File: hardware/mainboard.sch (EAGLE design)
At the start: 80 parts, among them IC1 ATMEGA328, IC10 HM628512A_DIL32, IC11 HM628512A_DIL32, IC12 7805TV, IC13 DS1210, IC14 6N138, IC3 TLC074, IC4 74HCT04N, IC5 74HC238N, IC6 74HCT573N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

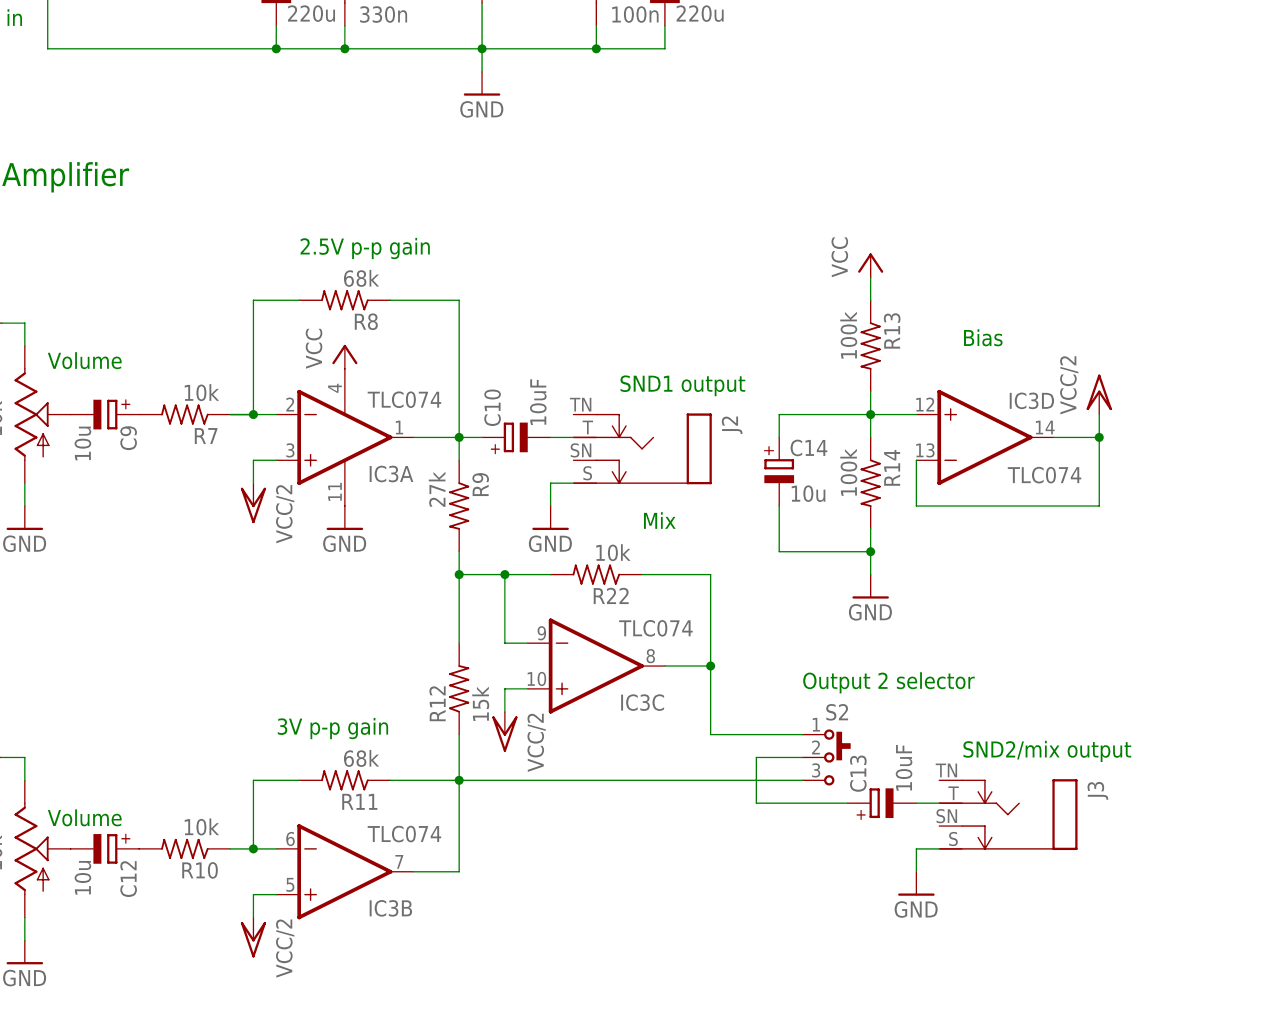
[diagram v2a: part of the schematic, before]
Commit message: Add small caps in feedback path for noise reduction and stability
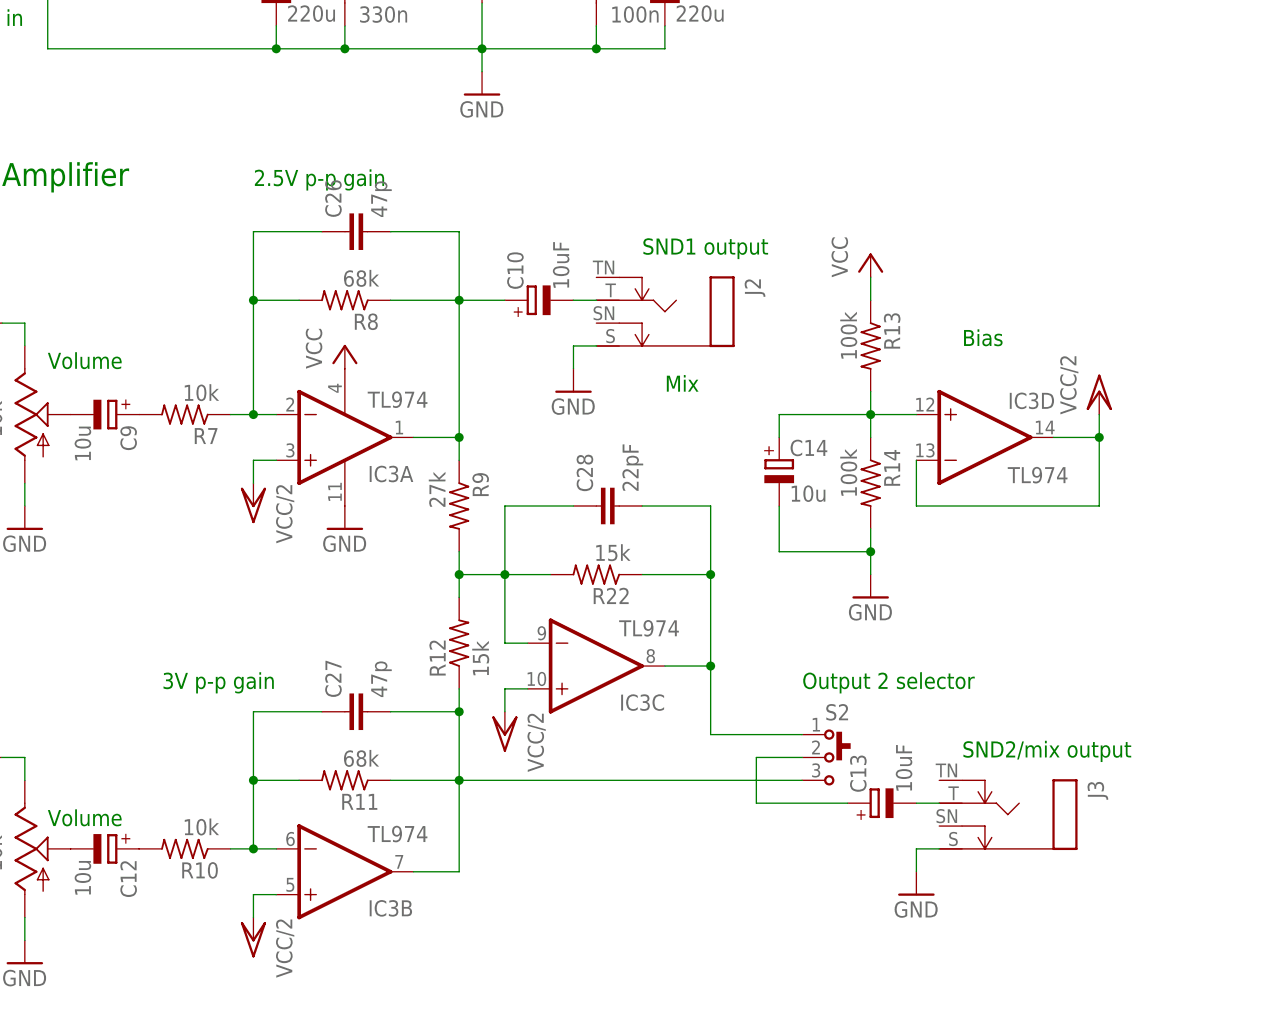
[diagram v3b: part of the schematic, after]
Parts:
- added C26, C27: 47p, capacitor-wima:C2.5/2
- added C28: 22pF, capacitor-wima:C2.5/2
- IC3: value TLC074 -> TL974
- R22: value 10k -> 15k
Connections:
- net N$14: now also C28.1
- net N$18: now also C26.1
- net N$24: now also C27.1
- net N$25: now also C26.2
- net N$26: now also C28.2
- net N$36: now also C27.2
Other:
- moved on the sheet: C10, J2, R12
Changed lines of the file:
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@@
 <part name="R12" library="rcl" deviceset="R-US_" device="0207/7" value="15k"/>
 <part name="R9" library="rcl" deviceset="R-US_" device="0207/7" value="27k"/>
-<part name="IC3" library="linear" deviceset="TL074" device="P" value="TLC074"/>
+<part name="IC3" library="linear" deviceset="TL074" device="P" value="TL974"/>
 <part name="R8" library="rcl" deviceset="R-US_" device="0207/7" value="68k"/>
 <part name="R7" library="rcl" deviceset="R-US_" device="0207/7" value="10k"/>
@@
 <part name="R16" library="rcl" deviceset="R-US_" device="0207/7" value="4.7k"/>
 <part name="D1" library="gm-diodes" deviceset="1N400X" device=".3"/>
-<part name="R22" library="rcl" deviceset="R-US_" device="0207/7" value="10k"/>
+<part name="R22" library="rcl" deviceset="R-US_" device="0207/7" value="15k"/>
 <part name="P+7" library="supply1" deviceset="VCC/2" device=""/>
+<part name="C26" library="capacitor-wima" deviceset="C" device="2.5/2" value="47p"/>
+<part name="C27" library="capacitor-wima" deviceset="C" device="2.5/2" value="47p"/>
+<part name="C28" library="capacitor-wima" deviceset="C" device="2.5/2" value="22pF"/>
 </parts>
 <sheets>
@@
 <text x="116.84" y="-96.52" size="2.54" layer="91">FIltering caps</text>
 <text x="55.88" y="-119.38" size="1.778" layer="91">SND2/mix output</text>
-<text x="17.78" y="-78.74" size="1.778" layer="91">SND1 output</text>
+<text x="20.32" y="-63.5" size="1.778" layer="91">SND1 output</text>
 <text x="-68.58" y="-38.1" size="1.778" layer="91">8V or higher DC in</text>
 <text x="-45.72" y="-76.2" size="1.778" layer="91">Volume</text>
 <text x="-45.72" y="-127" size="1.778" layer="91">Volume</text>
 <text x="38.1" y="-111.76" size="1.778" layer="91">Output 2 selector</text>
-<text x="-17.78" y="-63.5" size="1.778" layer="91">2.5V p-p gain</text>
-<text x="-20.32" y="-116.84" size="1.778" layer="91">3V p-p gain</text>
-<text x="20.32" y="-93.98" size="1.778" layer="91">Mix</text>
+<text x="-22.86" y="-55.88" size="1.778" layer="91">2.5V p-p gain</text>
+<text x="-33.02" y="-111.76" size="1.778" layer="91">3V p-p gain</text>
+<text x="22.86" y="-78.74" size="1.778" layer="91">Mix</text>
 <text x="304.8" y="-152.4" size="2.54" layer="91" font="vector">4</text>
 <text x="228.6" y="-132.08" size="2.54" layer="91" font="vector">(c) 2014-2015 Johan Fjeldtvedt</text>
@@
 <attribute name="VALUE" x="160.782" y="29.21" size="1.778" layer="96" rot="R90"/>
 </instance>
-<instance part="R12" gate="G$1" x="0" y="-111.76" rot="R90"/>
+<instance part="R12" gate="G$1" x="0" y="-106.68" rot="R90"/>
 <instance part="R9" gate="G$1" x="0" y="-91.44" smashed="yes" rot="R270">
 <attribute name="NAME" x="1.4986" y="-87.63" size="1.778" layer="95" rot="R270"/>
@@
 <instance part="R8" gate="G$1" x="-12.7" y="-68.58" rot="R180"/>
 <instance part="R7" gate="G$1" x="-30.48" y="-81.28" rot="R180"/>
-<instance part="C10" gate="G$1" x="5.08" y="-83.82" rot="R90"/>
+<instance part="C10" gate="G$1" x="7.62" y="-68.58" rot="R90"/>
 <instance part="R11" gate="G$1" x="-12.7" y="-121.92" rot="R180"/>
 <instance part="R10" gate="G$1" x="-30.48" y="-129.54" rot="R180"/>
@@
 <instance part="H3" gate="G$1" x="142.24" y="-149.86"/>
 <instance part="H4" gate="G$1" x="142.24" y="-154.94"/>
-<instance part="J2" gate="G$1" x="25.4" y="-86.36" rot="R180"/>
+<instance part="J2" gate="G$1" x="27.94" y="-71.12" rot="R180"/>
 <instance part="J3" gate="G$1" x="66.04" y="-127" rot="R180"/>
 <instance part="VR1" gate="L" x="-48.26" y="-81.28"/>
@@
 <attribute name="NAME" x="40.64" y="-115.2525" size="1.778" layer="95" ratio="10"/>
 </instance>
-<instance part="GND22" gate="1" x="10.16" y="-93.98"/>
+<instance part="GND22" gate="1" x="12.7" y="-78.74"/>
 <instance part="GND25" gate="1" x="50.8" y="-134.62"/>
 <instance part="GND8" gate="1" x="210.82" y="-73.66"/>
@@
 <instance part="R22" gate="G$1" x="15.24" y="-99.06" rot="R180"/>
 <instance part="P+7" gate="G$1" x="5.08" y="-116.84" rot="R180"/>
+<instance part="C26" gate="G$1" x="-12.7" y="-60.96" rot="R90"/>
+<instance part="C27" gate="G$1" x="-12.7" y="-114.3" rot="R90"/>
+<instance part="C28" gate="G$1" x="15.24" y="-91.44" rot="R90"/>
 </instances>
 <busses>
@@
 <segment>
 <pinref part="GND22" gate="1" pin="GND"/>
-<wire x1="10.16" y1="-88.9" x2="12.7" y2="-88.9" width="0.1524" layer="91"/>
+<wire x1="12.7" y1="-73.66" x2="15.24" y2="-73.66" width="0.1524" layer="91"/>
 <pinref part="J2" gate="G$1" pin="S"/>
-<wire x1="10.16" y1="-91.44" x2="10.16" y2="-88.9" width="0.1524" layer="91"/>
+<wire x1="12.7" y1="-76.2" x2="12.7" y2="-73.66" width="0.1524" layer="91"/>
 </segment>
 <segment>
@@
 <segment>
 <pinref part="R9" gate="G$1" pin="1"/>
-<pinref part="C10" gate="G$1" pin="+"/>
-<wire x1="0" y1="-83.82" x2="2.54" y2="-83.82" width="0.1524" layer="91"/>
 <wire x1="0" y1="-86.36" x2="0" y2="-83.82" width="0.1524" layer="91"/>
 <junction x="0" y="-83.82"/>
@@
 <pinref part="IC3" gate="A" pin="OUT"/>
 <wire x1="-5.08" y1="-83.82" x2="0" y2="-83.82" width="0.1524" layer="91"/>
+<pinref part="C26" gate="G$1" pin="2"/>
+<wire x1="-7.62" y1="-60.96" x2="0" y2="-60.96" width="0.1524" layer="91"/>
+<wire x1="0" y1="-60.96" x2="0" y2="-68.58" width="0.1524" layer="91"/>
+<junction x="0" y="-68.58"/>
+<pinref part="C10" gate="G$1" pin="+"/>
+<wire x1="0" y1="-68.58" x2="5.08" y2="-68.58" width="0.1524" layer="91"/>
 </segment>
 </net>
@@
 <pinref part="J2" gate="G$1" pin="T"/>
 <pinref part="C10" gate="G$1" pin="-"/>
-<wire x1="10.16" y1="-83.82" x2="12.7" y2="-83.82" width="0.1524" layer="91"/>
+<wire x1="12.7" y1="-68.58" x2="15.24" y2="-68.58" width="0.1524" layer="91"/>
 </segment>
 </net>
@@
 <pinref part="R12" gate="G$1" pin="2"/>
 <pinref part="R9" gate="G$1" pin="2"/>
-<wire x1="0" y1="-106.68" x2="0" y2="-99.06" width="0.1524" layer="91"/>
+<wire x1="0" y1="-101.6" x2="0" y2="-99.06" width="0.1524" layer="91"/>
 <pinref part="IC3" gate="C" pin="-IN"/>
 <wire x1="0" y1="-99.06" x2="0" y2="-96.52" width="0.1524" layer="91"/>
@@
 <junction x="5.08" y="-99.06"/>
 <junction x="0" y="-99.06"/>
+<wire x1="5.08" y1="-99.06" x2="5.08" y2="-91.44" width="0.1524" layer="91"/>
+<pinref part="C28" gate="G$1" pin="1"/>
+<wire x1="5.08" y1="-91.44" x2="12.7" y2="-91.44" width="0.1524" layer="91"/>
 </segment>
 </net>
@@
 <wire x1="22.86" y1="-109.22" x2="27.94" y2="-109.22" width="0.1524" layer="91"/>
 <junction x="27.94" y="-109.22"/>
+<pinref part="C28" gate="G$1" pin="2"/>
+<wire x1="20.32" y1="-91.44" x2="27.94" y2="-91.44" width="0.1524" layer="91"/>
+<wire x1="27.94" y1="-91.44" x2="27.94" y2="-99.06" width="0.1524" layer="91"/>
+<junction x="27.94" y="-99.06"/>
 </segment>
 </net>
@@
 <segment>
 <pinref part="R7" gate="G$1" pin="1"/>
-<wire x1="-25.4" y1="-81.28" x2="-22.86" y2="-81.28" width="0.1524" layer="91"/>
 <wire x1="-22.86" y1="-81.28" x2="-22.86" y2="-68.58" width="0.1524" layer="91"/>
 <pinref part="R8" gate="G$1" pin="2"/>
@@
 <junction x="-22.86" y="-81.28"/>
 <wire x1="-22.86" y1="-81.28" x2="-20.32" y2="-81.28" width="0.1524" layer="91"/>
+<wire x1="-22.86" y1="-68.58" x2="-22.86" y2="-60.96" width="0.1524" layer="91"/>
+<pinref part="C26" gate="G$1" pin="1"/>
+<wire x1="-22.86" y1="-60.96" x2="-15.24" y2="-60.96" width="0.1524" layer="91"/>
+<junction x="-22.86" y="-68.58"/>
 </segment>
 </net>
@@
 <wire x1="-22.86" y1="-121.92" x2="-17.78" y2="-121.92" width="0.1524" layer="91"/>
 <junction x="-22.86" y="-129.54"/>
+<pinref part="C27" gate="G$1" pin="1"/>
+<wire x1="-15.24" y1="-114.3" x2="-22.86" y2="-114.3" width="0.1524" layer="91"/>
+<wire x1="-22.86" y1="-114.3" x2="-22.86" y2="-121.92" width="0.1524" layer="91"/>
+<junction x="-22.86" y="-121.92"/>
 </segment>
 </net>
@@
 <wire x1="0" y1="-132.08" x2="0" y2="-121.92" width="0.1524" layer="91"/>
 <pinref part="R12" gate="G$1" pin="1"/>
-<wire x1="0" y1="-121.92" x2="0" y2="-116.84" width="0.1524" layer="91"/>
+<wire x1="0" y1="-121.92" x2="0" y2="-114.3" width="0.1524" layer="91"/>
 <junction x="0" y="-121.92"/>
+<wire x1="0" y1="-114.3" x2="0" y2="-111.76" width="0.1524" layer="91"/>
 <wire x1="-5.08" y1="-132.08" x2="0" y2="-132.08" width="0.1524" layer="91"/>
 <pinref part="S2" gate="G$1" pin="3"/>
 <wire x1="0" y1="-121.92" x2="38.1" y2="-121.92" width="0.1524" layer="91"/>
-</segment>
-</net>
+<pinref part="C27" gate="G$1" pin="2"/>
+<wire x1="-7.62" y1="-114.3" x2="0" y2="-114.3" width="0.1524" layer="91"/>
+<junction x="0" y="-114.3"/>
+</segment>
+</net>

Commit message: New battery backup circuit
The DS1210 is expensive and found to not really be needed here, so it has been
replaced by a discrete transistor circuit.

The op-amp used for the bias voltage buffer in the audio amplifier is now used
for buffering the battery voltage instead. Its output is now connected to ADC5
of the ATmega to allow for reading the battery voltage.
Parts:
- removed IC13: DS1210, maxim-custom:DS1210-8PDIP
- removed Q1, Q2: BC557, transistor-pnp:BC557
- added D3, D4: 1N914.3, gm-diodes:1N914.3
- added T2, T3: BC547, transistor:BC547
- R15: value 220 -> 15k
- R16: value 4.7k -> 220
- R17: value 220 -> 4.7k
- R18: value 100k -> 220
- R19: value 100k -> 4.7k
- R20: value 1k -> 27k
- R21: value 1k -> 4.7k
- R22: value 15k -> 4.7k
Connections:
- removed net N$29: IC13.!CEO, R20.2, R21.2
- removed net N$37: Q2.B, R21.1
- removed net VCC/2: IC3A.+IN, IC3B.+IN, IC3C.+IN, IC3D.-IN, IC3D.OUT
- new net VBAT: IC1.PC5(ADC5/SCL), IC3D.-IN, IC3D.OUT
- net CE1: now also T2.E; no longer Q1.E
- net CE2: now also T3.E; no longer Q2.E
- net GND: now also IC4E.I, IC4F.I, R17.1, R19.2; no longer IC13.!CE, IC13.GND, IC13.VBAT2, R16.1
- net MEM1_CE: now also R21.2, T2.C; no longer Q1.C, R18.2
- net MEM2_CE: now also R22.2, T3.C; no longer Q2.C, R19.2
- net MEM_VCC: now also D3.C, D4.C, R21.1, R22.1; no longer IC13.TOL, IC13.VCCO, R18.1, R19.1
- net MIDI_IN: now also R18.1; no longer R17.1
- net MIDI_PIN_4: now also R16.1; no longer R15.1
- net N$14: now also R15.2; no longer R22.2
- net N$19: now also D3.A, IC3D.+IN; no longer IC13.VBAT1
- net N$20: now also R17.2; no longer R16.2
- net N$26: now also R15.1; no longer R22.1
- net N$28: now also IC3A.+IN, IC3B.+IN, IC3C.+IN; no longer IC3D.+IN
- net N$33: now also R19.1, R20.2, T2.B, T3.B; no longer Q1.B, R20.1
- net N$34: now also R16.2; no longer R15.2
- net VCC: now also D4.A, R18.2, R20.1; no longer IC13.VCCI, R17.2
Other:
- moved on the sheet: BAT1, C1, C11, C12, C13, C14, C2, C27, C28, C3, C4, D1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

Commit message: Hardware: connect inverted R/W to output enable of 2a03 latch
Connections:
- new net N$29: IC4E.O, IC6A.OC
- net GND: now also IC9A.6D, IC9A.7D, IC9A.8D; no longer IC4E.I, IC6A.OC
- net R/W: now also IC4E.I
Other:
- note added: "6"
- note removed: "4"
- moved on the sheet: BAT1, C15, C16, C17, C18, C19, C20, C21, C22, C23, C24, C25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

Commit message: added sch and brd files for hardware
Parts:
- C26, C27: value 47p -> 22pF
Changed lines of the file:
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@@
 <part name="D1" library="gm-diodes" deviceset="1N400X" device=".3"/>
 <part name="R15" library="rcl" deviceset="R-US_" device="0207/7" value="15k"/>
-<part name="C26" library="capacitor-wima" deviceset="C" device="2.5/2" value="47p"/>
-<part name="C27" library="capacitor-wima" deviceset="C" device="2.5/2" value="47p"/>
+<part name="C26" library="capacitor-wima" deviceset="C" device="2.5/2" value="22pF"/>
+<part name="C27" library="capacitor-wima" deviceset="C" device="2.5/2" value="22pF"/>
 <part name="C28" library="capacitor-wima" deviceset="C" device="2.5/2" value="22pF"/>
 <part name="R21" library="rcl" deviceset="R-US_" device="0207/7" value="4.7k"/>

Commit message: Main board v0.9: fix memory backup, new MIDI connector, BOM fixes
The discrete memory backup circuit turned out to be too fragile. The old
DS1210 based design is back, but it is now also used to provide the CPU
RESET signal to further reduce the possibility of memory corruption. The
battery voltage is still being connected (through a buffer) to the
Atmega for being able to check the battery voltage.

The MIDI connector that was used previously is not being stocked at
Mouser any more, so it has been replaced by one that is.

A couple of fixes have been done to the BOM, replacing out of stock
components with drop-in replacements (a resistor and the 74'238).

This should hopefully be the last revision of the main board...
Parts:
- removed C7: 10n, rcl:C-EU025-025X050
- removed D3, D4: 1N914.3, gm-diodes:1N914.3
- removed J4: MIDI_CONN_FEMALE_SUPPORT, SparkFun-Connectors:MIDI_CONN_FEMALE_SUPPORT
- removed R1: 4.7k, rcl:R-US_0207/7
- removed T2, T3: BC547, transistor:BC547
- added IC13: DS1210-8PDIP, maxim-custom:DS1210-8PDIP
- added Q1, Q2: BC557, transistor-pnp:BC557
- added X2: MAB5SH, con-hirschmann:MAB5SH
- R19: value 4.7k -> 1k
- R20: value 27k -> 1k
- R21, R22: value 4.7k -> 100k
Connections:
- removed net N$19: BAT1.+, D3.A, IC3D.+IN
- new net N$37: Q1.B, R19.1
- new net N$38: Q2.B, R20.1
- new net N$39: BAT1.+, IC13.VBAT1, IC3D.+IN
- net CE1: now also Q1.E; no longer T2.E
- net CE2: now also Q2.E; no longer T3.E
- net GND: now also IC13.!CE, IC13.GND, IC13.VBAT2, X2.PE; no longer C7.2, IC4F.I, R19.2
- net MEM1_CE: now also Q2.C; no longer T2.C
- net MEM2_CE: now also Q1.C; no longer T3.C
- net MEM_VCC: now also IC13.TOL, IC13.VCCO; no longer D3.C, D4.C
- net MIDI_PIN_4: now also X2.4; no longer J4.CSRC
- net MIDI_PIN_5: now also X2.5; no longer J4.CSNK
- net N$33: now also IC13.!CEO, IC4F.I, R19.2; no longer R19.1, T2.B, T3.B
- net RESET: now also IC4F.O; no longer C7.1, R1.2
- net VCC: now also IC13.VCCI; no longer D4.A, R1.1, R20.1
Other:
- note added: "(c) 2014-2016 Johan Fjeldtvedt"
- note added: "v0.9"
- note removed: "(c) 2014-2015 Johan Fjeldtvedt"
- note removed: "6"
- moved on the sheet: BAT1, IC3D, IC4F, R19, R20, R21, R22
